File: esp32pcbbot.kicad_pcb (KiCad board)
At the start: 2 copper layers, 110 x 170 mm, 44 parts, among them IC1 BMI055, J1 TB002-500-02BE, J2 TB002-500-02BE, J3 TB002-500-02BE, J4 215299-4, J5 SSQ-120-01-L-D, J6 215299-4, Q1 2N7002, Q2 2N7002, Q3 Q_Photo_NPN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

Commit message: try try try again
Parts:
- moved R1 3.00 mm to (77.0, 32.0)
- moved R2 3.00 mm to (59.0, 32.0)
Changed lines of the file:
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@@
   )
   (module Resistor_SMD:R_0603_1608Metric (layer F.Cu)
-    (at 59 29 180)
+    (at 59 32 180)
     (descr "Resistor SMD 0603 (1608 Metric), square (rectangular) end terminal, IPC_7351 nominal, (Body size source: IPC-SM-782 page 72, https://www.pcb-3d.com/wordpress/wp-content/uploads/ipc-sm-782a_amendment_1_and_2.pdf), generated with kicad-footprint-generator")
     (tags resistor)
@@
   )
   (module Resistor_SMD:R_0603_1608Metric (layer F.Cu)
-    (at 77 29)
+    (at 77 32)
     (descr "Resistor SMD 0603 (1608 Metric), square (rectangular) end terminal, IPC_7351 nominal, (Body size source: IPC-SM-782 page 72, https://www.pcb-3d.com/wordpress/wp-content/uploads/ipc-sm-782a_amendment_1_and_2.pdf), generated with kicad-footprint-generator")
     (tags resistor)

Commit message: finished up the routing stuff
I think its ready to be ordered!!!
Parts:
- moved R1 18.0 mm to (59.0, 31.0), turned to 180 degrees
- moved R2 3.00 mm to (59.0, 29.0), turned to 0 degrees
- moved USB1 1.00 mm to (69.0, 27.5)
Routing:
- net GND: track 0.00 -> 926.3 mm, vias 0 -> 36
- net +5V: track 0.00 -> 357.4 mm, vias 0 -> 2
- net +3V3: track 0.00 -> 224.6 mm, vias 0 -> 6
- net VBUS: track 0.00 -> 207.4 mm, vias 0 -> 1
- net Net-(S2-Pad2): track 0.00 -> 167.0 mm, vias 0 -> 1
- net M1A: track 0.00 -> 164.5 mm, vias 0 -> 2
- net 12Y: track 0.00 -> 141.6 mm
- net VCC: track 0.00 -> 135.9 mm
- net Net-(S2-Pad5): track 0.00 -> 134.8 mm, vias 0 -> 1
- net BOOT: track 0.00 -> 131.1 mm
- net M1B: track 0.00 -> 127.8 mm
- net 11Y: track 0.00 -> 127.2 mm
- net EN: track 0.00 -> 126.8 mm, vias 0 -> 3
- net 10Y: track 0.00 -> 107.2 mm
- net 9Y: track 0.00 -> 105.6 mm, vias 0 -> 1
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- added copper zone on B.Cu, net GND

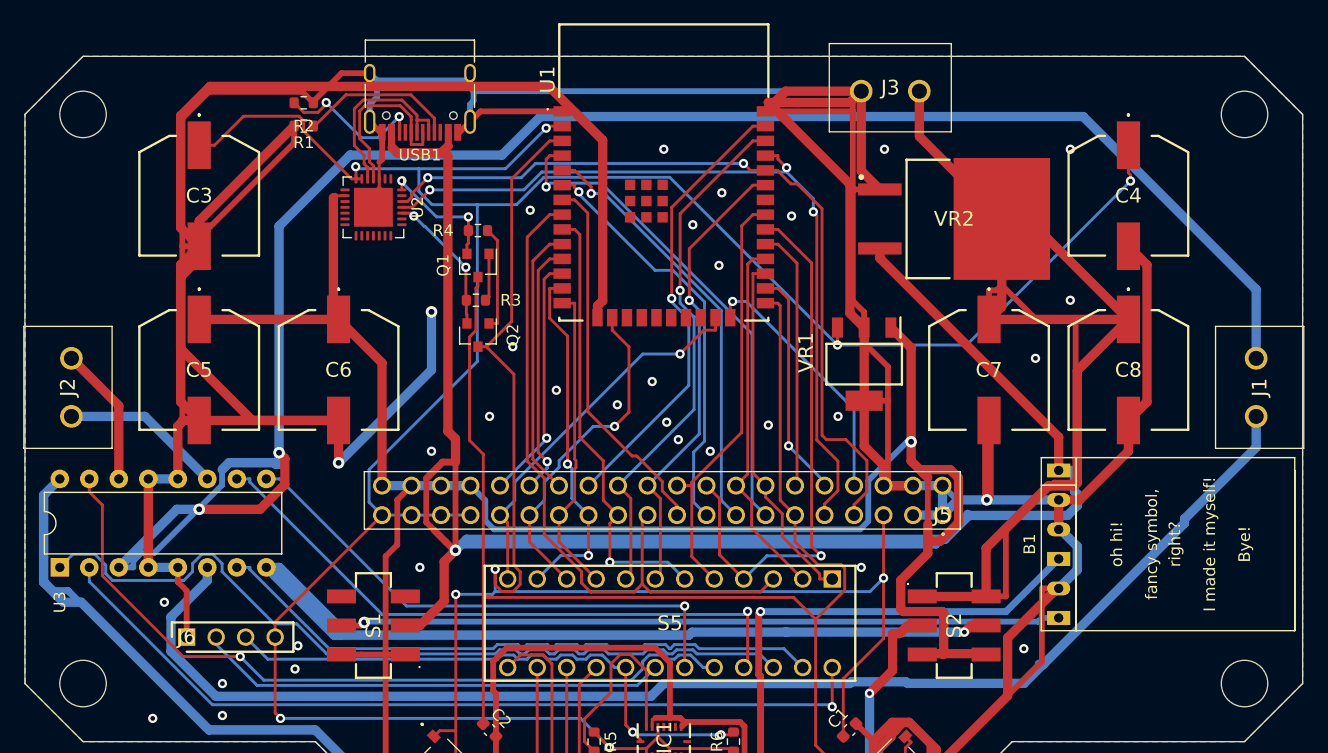
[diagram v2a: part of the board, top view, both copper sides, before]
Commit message: fixed infuriating board dimensions
switched from 59 to 60 mm
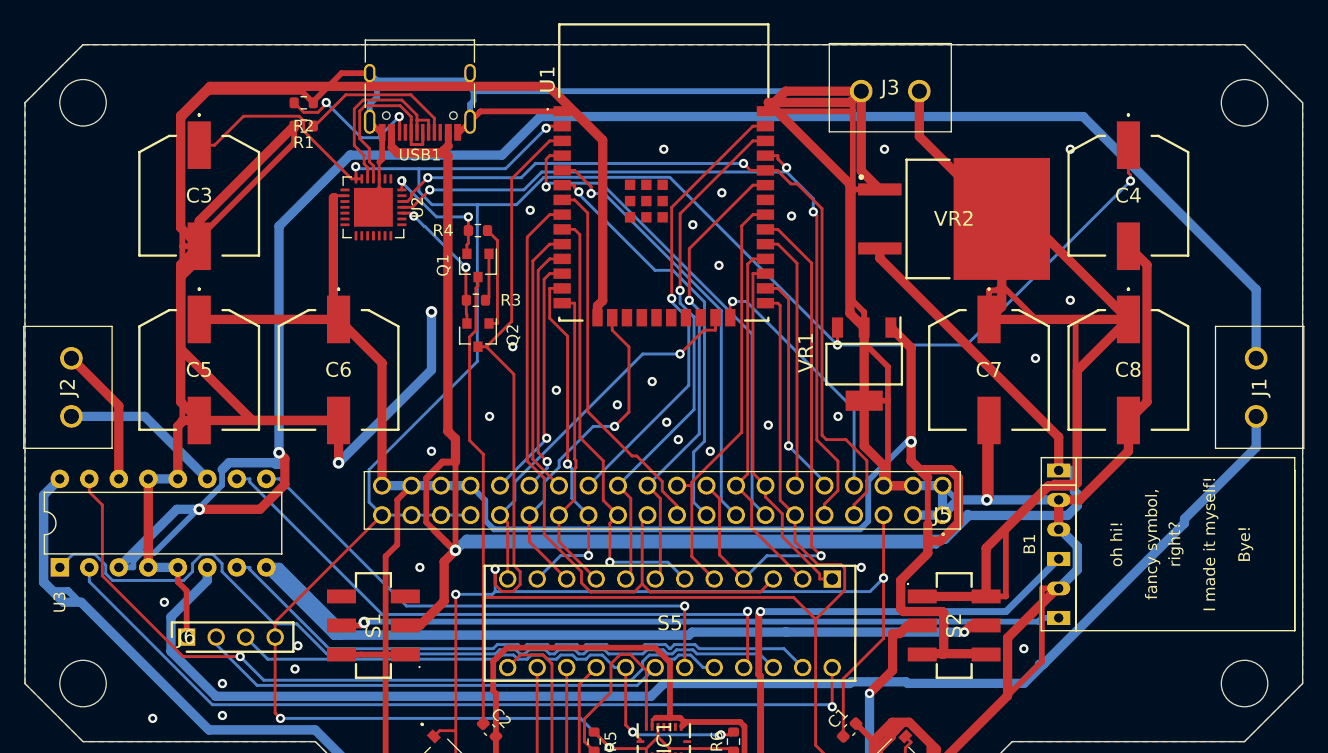
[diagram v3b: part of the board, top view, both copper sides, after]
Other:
- board size 110 x 170 mm -> 110 x 171 mm
